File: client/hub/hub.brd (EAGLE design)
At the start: 45.7 x 39.4 mm, 12 parts

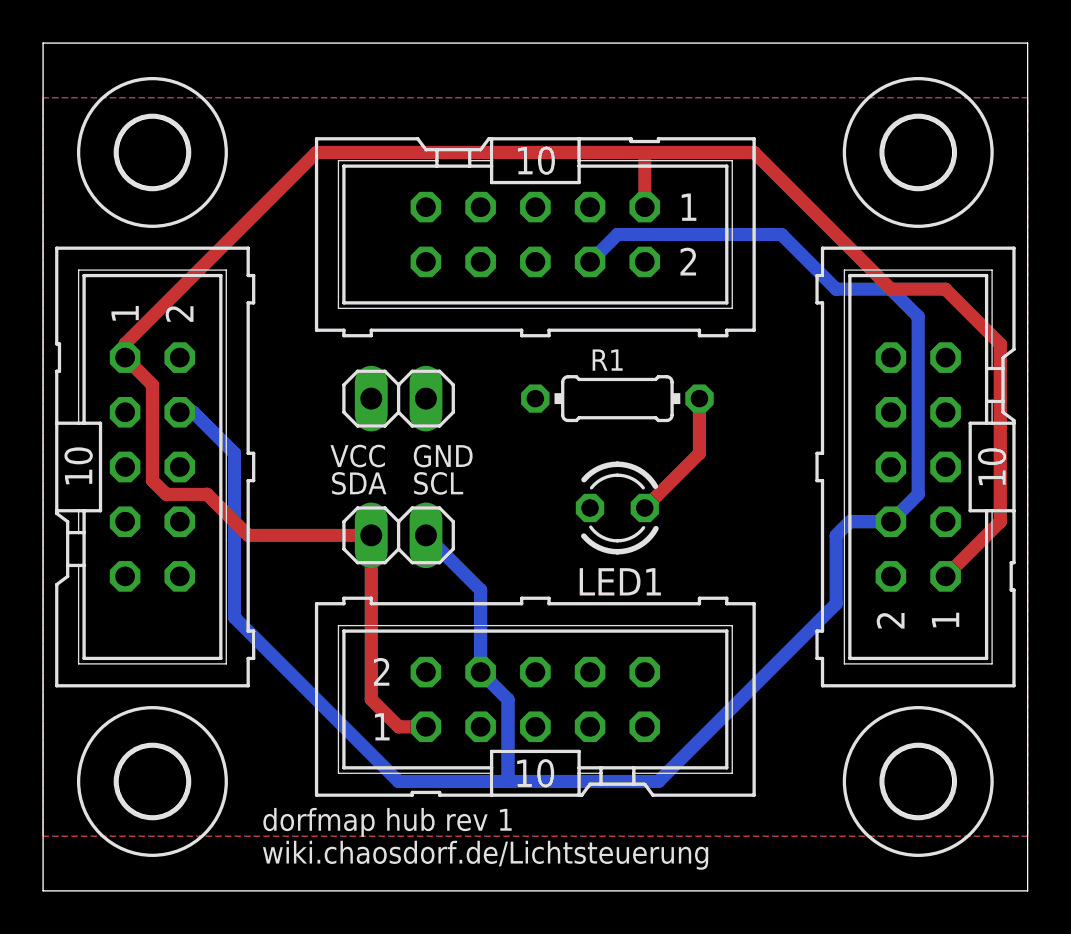
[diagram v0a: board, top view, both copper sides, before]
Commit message: hub: bigger solder pads for the damn connectors
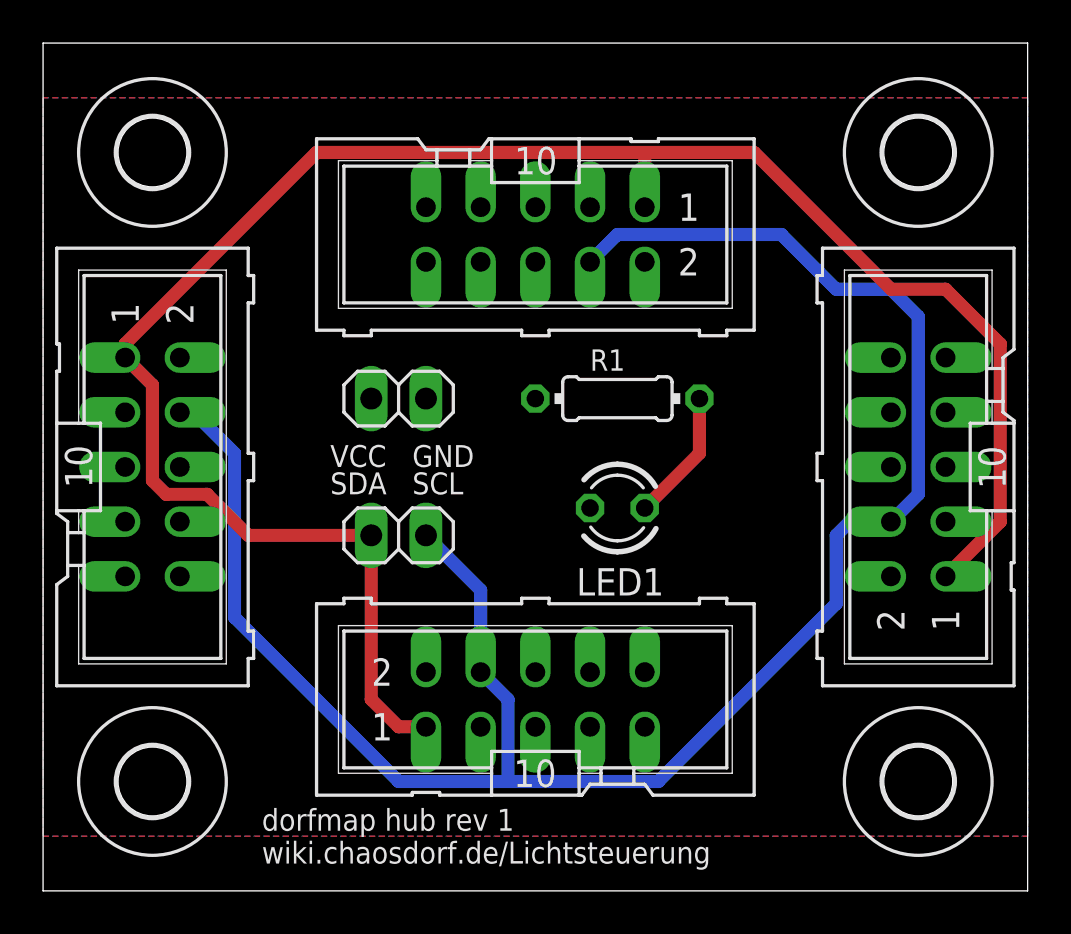
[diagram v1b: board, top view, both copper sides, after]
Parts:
- SV1, SV2, SV3, SV4: device con-harting-ml:ML10 -> con-harting-ml-derf:ML10
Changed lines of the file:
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@@
 </autorouter>
 <elements>
-<element name="SV1" library="con-harting-ml" package="ML10" value="SI2C" x="5.08" y="19.685" smashed="yes" rot="R270">
+<element name="SV1" library="con-harting-ml-derf" package="ML10" value="SI2C" x="5.08" y="19.685" smashed="yes" rot="R270">
 <attribute name="OC_NEWARK" value="unknown" x="0" y="-23.495" size="1.778" layer="27" rot="R270" display="off"/>
 <attribute name="MPN" value="" x="0" y="-23.495" size="1.778" layer="27" rot="R270" display="off"/>
@@
 <attribute name="VALUE" x="13.97" y="19.685" size="1.27" layer="27"/>
 </element>
-<element name="SV2" library="con-harting-ml" package="ML10" value="SI2C" x="40.64" y="19.685" smashed="yes" rot="R90">
+<element name="SV2" library="con-harting-ml-derf" package="ML10" value="SI2C" x="40.64" y="19.685" smashed="yes" rot="R90">
 <attribute name="MPN" value="" x="40.64" y="19.685" size="1.778" layer="27" rot="R90" display="off"/>
 <attribute name="MF" value="" x="40.64" y="19.685" size="1.778" layer="27" rot="R90" display="off"/>
@@
 <attribute name="VALUE" x="35.56" y="19.685" size="1.778" layer="27" ratio="10" rot="R90"/>
 </element>
-<element name="SV3" library="con-harting-ml" package="ML10" value="SI2C" x="22.86" y="30.48" smashed="yes" rot="R180">
+<element name="SV3" library="con-harting-ml-derf" package="ML10" value="SI2C" x="22.86" y="30.48" smashed="yes" rot="R180">
 <attribute name="MPN" value="" x="22.86" y="30.48" size="1.778" layer="27" rot="R180" display="off"/>
 <attribute name="MF" value="" x="22.86" y="30.48" size="1.778" layer="27" rot="R180" display="off"/>
@@
 <attribute name="VALUE" x="22.86" y="25.4" size="1.778" layer="27" ratio="10" rot="R180"/>
 </element>
-<element name="SV4" library="con-harting-ml" package="ML10" value="SI2C" x="22.86" y="8.89" smashed="yes">
+<element name="SV4" library="con-harting-ml-derf" package="ML10" value="SI2C" x="22.86" y="8.89" smashed="yes">
 <attribute name="MPN" value="" x="22.86" y="8.89" size="1.778" layer="27" display="off"/>
 <attribute name="MF" value="" x="22.86" y="8.89" size="1.778" layer="27" display="off"/>
